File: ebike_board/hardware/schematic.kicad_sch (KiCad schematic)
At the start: 9 parts, among them J3 Connector_1, U1 ESP32-S3-DevKitC, U2 TJA1050_module

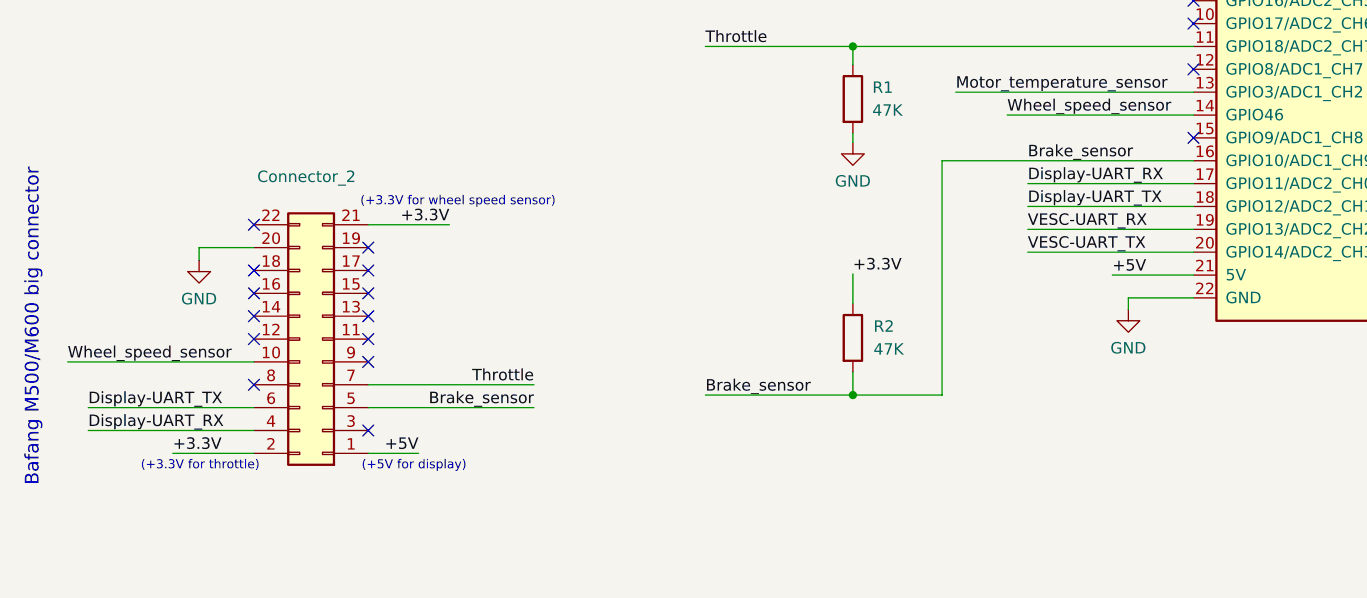
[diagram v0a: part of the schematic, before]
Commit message: Updated the schematics by removing the UART connection between the EBike board and the display
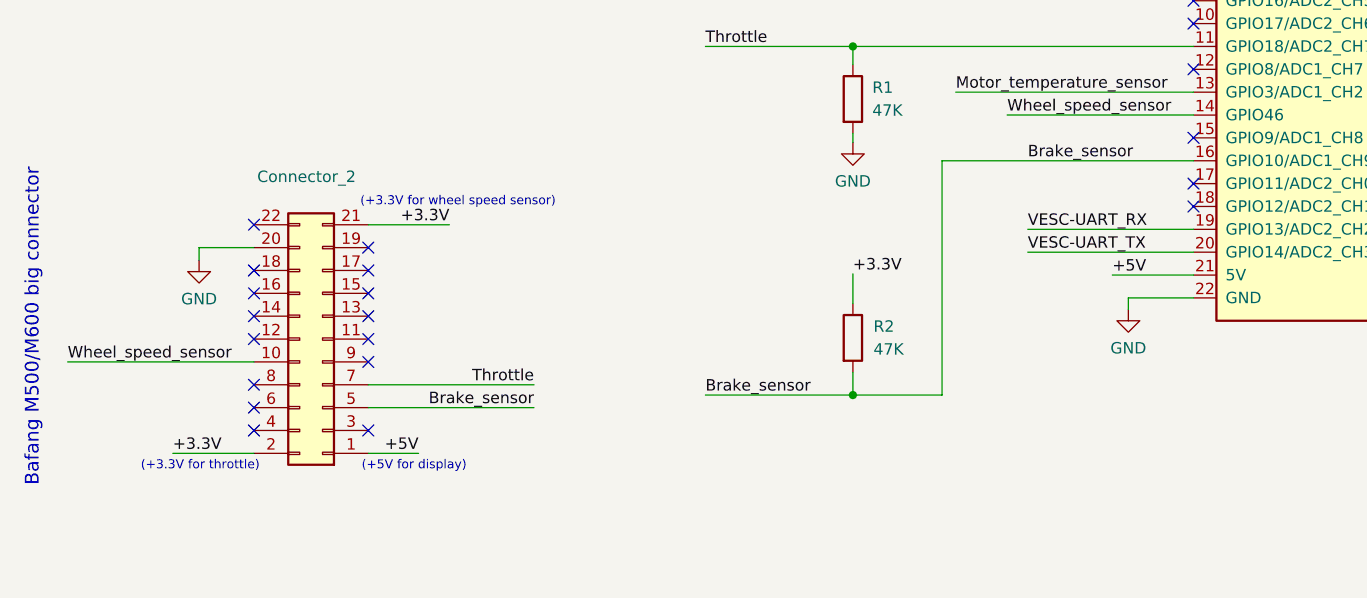
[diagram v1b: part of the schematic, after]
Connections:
- net Display-UART_RX: no longer names the net of Connector_2.4 (Pin_4)
- net Display-UART_RX: no longer U1.17 (GPIO11/ADC2_CH0)
- net Display-UART_TX: no longer names the net of Connector_2.6 (Pin_6)
- net Display-UART_TX: no longer U1.18 (GPIO12/ADC2_CH1)
- no-connect marks 50 -> 54
